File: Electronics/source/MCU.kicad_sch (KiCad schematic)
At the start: 48 parts, among them J1 Conn_01x05, J16 Conn_01x02, J2 Conn_01x03, J3 Conn_01x03, J4 Conn_01x05, J6 Conn_01x20, J7 Conn_01x20, SW10 SW_Push, SW11 SW_Push, SW12 SW_Push, SW13 SW_Push, SW14 SW_Coded, SW4 SW_Push, SW5 SW_SPDT, SW6 SW_SPDT, SW7 SW_SPDT, SW8 SW_Push, SW9 SW_Push, U1 STM32F030C8Tx, U4 FT231XS, U5 ADP122AUJZ-3.3-R7, Y1 ABL-32.000MHZ-B2

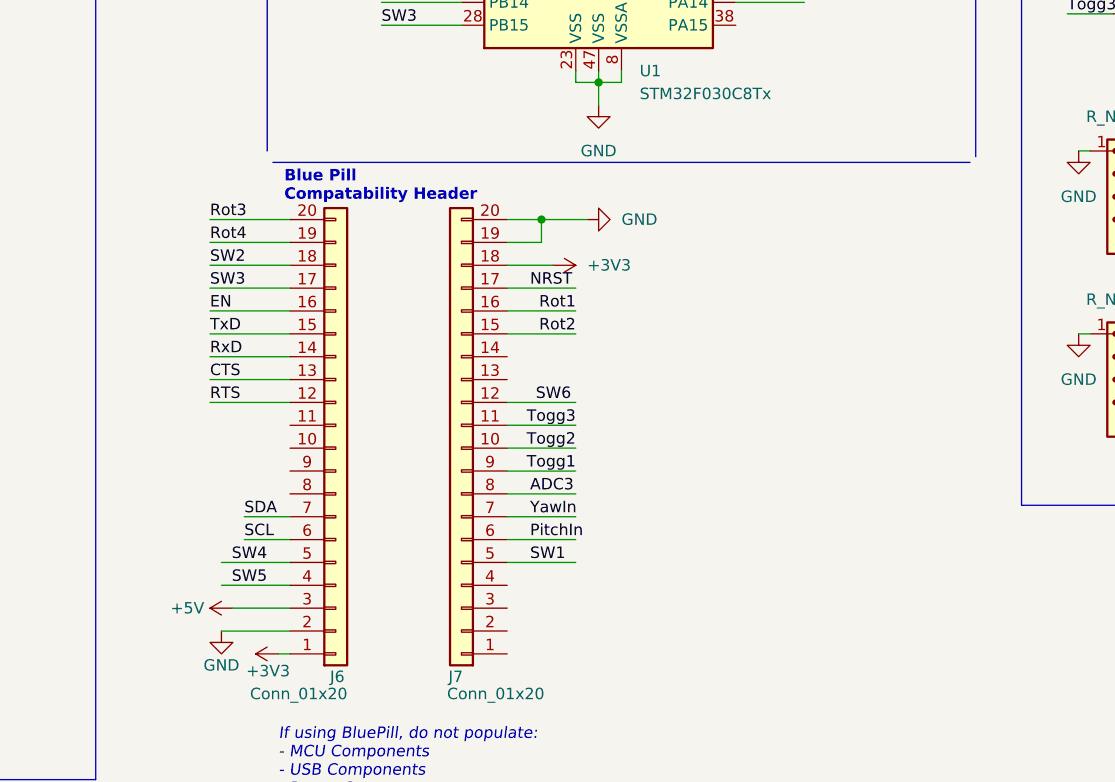
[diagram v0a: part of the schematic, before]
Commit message: Finished first layout of all boards
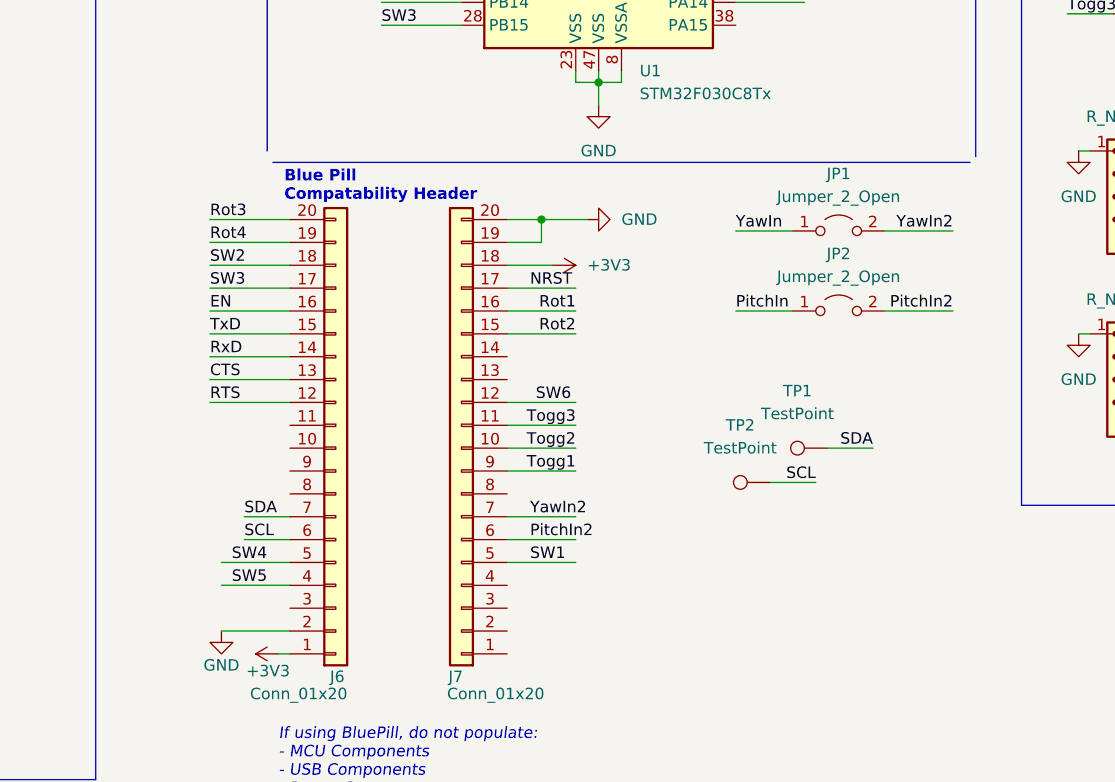
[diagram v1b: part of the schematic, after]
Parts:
- added JP1, JP2: Jumper_2_Open, Jumper:SolderJumper-2_P1.3mm_Open_TrianglePad1.0x1.5mm, symbol Jumper:Jumper_2_Open
- added TP1, TP2: TestPoint, TestPoint:TestPoint_Pad_D1.0mm, symbol Connector:TestPoint
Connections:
- net +5V: no longer J6.3 (Pin_3)
- net ADC3: no longer J7.8 (Pin_8)
- net PitchIn: now also JP2.1 (A); no longer J7.6 (Pin_6)
- net SCL: now also TP2.1
- net SDA: now also TP1.1
- net YawIn: now also JP1.1 (A); no longer J7.7 (Pin_7)
- new net PitchIn2: J7.6 (Pin_6), JP2.2 (B)
- new net YawIn2: J7.7 (Pin_7), JP1.2 (B)
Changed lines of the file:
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@@
-    (stroke (width 0) (type default) (color 0 0 0 0))
-  )
-  (wire (pts (xy 111.76 173.99) (xy 105.41 173.99))
     (stroke (width 0) (type default) (color 0 0 0 0))
   )
@@
     (stroke (width 0) (type default) (color 0 0 0 0))
   )
+  (wire (pts (xy 161.29 140.97) (xy 167.64 140.97))
+    (stroke (width 0) (type default) (color 0 0 0 0))
+  )
   (wire (pts (xy 121.92 66.04) (xy 130.81 66.04))
     (stroke (width 0) (type default) (color 0 0 0 0))
@@
     (stroke (width 0) (type default) (color 0 0 0 0))
   )
+  (wire (pts (xy 177.8 132.08) (xy 185.42 132.08))
+    (stroke (width 0) (type default) (color 0 0 0 0))
+  )
   (wire (pts (xy 161.29 73.66) (xy 168.91 73.66))
     (stroke (width 0) (type default) (color 0 0 0 0))
@@
     (stroke (width 0) (type default) (color 0 0 0 0))
   )
+  (wire (pts (xy 165.1 160.02) (xy 170.18 160.02))
+    (stroke (width 0) (type default) (color 0 0 0 0))
+  )
   (wire (pts (xy 161.29 106.68) (xy 168.91 106.68))
     (stroke (width 0) (type default) (color 0 0 0 0))
@@
     (stroke (width 0) (type default) (color 0 0 0 0))
   )
+  (wire (pts (xy 177.8 140.97) (xy 185.42 140.97))
+    (stroke (width 0) (type default) (color 0 0 0 0))
+  )
   (wire (pts (xy 194.31 44.45) (xy 203.2 44.45))
     (stroke (width 0) (type default) (color 0 0 0 0))
@@
     (stroke (width 0) (type default) (color 0 0 0 0))
   )
+  (wire (pts (xy 161.29 132.08) (xy 167.64 132.08))
+    (stroke (width 0) (type default) (color 0 0 0 0))
+  )
   (wire (pts (xy 102.87 135.89) (xy 111.76 135.89))
     (stroke (width 0) (type default) (color 0 0 0 0))
@@
     (stroke (width 0) (type default) (color 0 0 0 0))
   )
+  (wire (pts (xy 171.45 156.21) (xy 176.53 156.21))
+    (stroke (width 0) (type default) (color 0 0 0 0))
+  )
   (wire (pts (xy 121.92 73.66) (xy 130.81 73.66))
     (stroke (width 0) (type default) (color 0 0 0 0))
@@
   )
   (wire (pts (xy 148.59 115.57) (xy 146.05 115.57))
-    (stroke (width 0) (type default) (color 0 0 0 0))
-  )
-  (wire (pts (xy 135.89 161.29) (xy 143.51 161.29))
     (stroke (width 0) (type default) (color 0 0 0 0))
   )
@@
     (effects (font (size 1.27 1.27)) (justify left bottom))
   )
+  (label "PitchIn2" (at 185.42 140.97 180)
+    (effects (font (size 1.27 1.27)) (justify right bottom))
+  )
   (label "Togg2" (at 143.51 156.21 180)
     (effects (font (size 1.27 1.27)) (justify right bottom))
   )
-  (label "PitchIn" (at 138.43 166.37 0)
+  (label "PitchIn2" (at 138.43 166.37 0)
     (effects (font (size 1.27 1.27)) (justify left bottom))
   )
@@
     (effects (font (size 1.27 1.27)) (justify right bottom))
   )
-  (label "YawIn" (at 138.43 163.83 0)
+  (label "YawIn" (at 161.29 132.08 0)
+    (effects (font (size 1.27 1.27)) (justify left bottom))
+  )
+  (label "SCL" (at 170.18 160.02 180)
+    (effects (font (size 1.27 1.27)) (justify right bottom))
+  )
+  (label "YawIn2" (at 138.43 163.83 0)
     (effects (font (size 1.27 1.27)) (justify left bottom))
   )
@@
     (effects (font (size 1.27 1.27)) (justify left bottom))
   )
+  (label "YawIn2" (at 185.42 132.08 180)
+    (effects (font (size 1.27 1.27)) (justify right bottom))
+  )
   (label "USB_DM" (at 76.2 96.52 0)
     (effects (font (size 1.27 1.27)) (justify left bottom))
@@
   (label "3v3Out" (at 29.21 144.78 0)
     (effects (font (size 1.27 1.27)) (justify left bottom))
+  )
+  (label "SDA" (at 176.53 156.21 180)
+    (effects (font (size 1.27 1.27)) (justify right bottom))
   )
   (label "GND" (at 203.2 27.94 180)
@@
     (effects (font (size 1.27 1.27)) (justify left bottom))
   )
-  (label "ADC3" (at 138.43 161.29 0)
-    (effects (font (size 1.27 1.27)) (justify left bottom))
-  )
   (label "SW6" (at 259.08 154.94 0)
+    (effects (font (size 1.27 1.27)) (justify left bottom))
+  )
+  (label "PitchIn" (at 161.29 140.97 0)
     (effects (font (size 1.27 1.27)) (justify left bottom))
   )
@@
   (label "SDA" (at 203.2 22.86 180)
     (effects (font (size 1.27 1.27)) (justify right bottom))
+  )
+  (symbol (lib_id "Connector:TestPoint") (at 165.1 160.02 90) (unit 1)
+    (in_bom yes) (on_board yes) (fields_autoplaced)
+    (property "Reference" "TP2" (id 0) (at 161.798 153.67 90))
+    (property "Value" "TestPoint" (id 1) (at 161.798 156.21 90))
+    (property "Footprint" "TestPoint:TestPoint_Pad_D1.0mm" (id 2) (at 165.1 154.94 0)
+      (effects (font (size 1.27 1.27)) hide)
+    )
+    (property "Datasheet" "~" (id 3) (at 165.1 154.94 0)
+      (effects (font (size 1.27 1.27)) hide)
+    )
+    (pin "1")
   )
   (symbol (lib_id "Device:R_Network05") (at 205.74 148.59 90) (mirror x) (unit 1)
@@
     (pin "2")
   )
+  (symbol (lib_id "Jumper:Jumper_2_Open") (at 172.72 140.97 0) (unit 1)
+    (in_bom yes) (on_board yes) (fields_autoplaced)
+    (property "Reference" "JP2" (id 0) (at 172.72 134.62 0))
+    (property "Value" "Jumper_2_Open" (id 1) (at 172.72 137.16 0))
+    (property "Footprint" "Jumper:SolderJumper-2_P1.3mm_Open_TrianglePad1.0x1.5mm" (id 2) (at 172.72 140.97 0)
+      (effects (font (size 1.27 1.27)) hide)
+    )
+    (property "Datasheet" "~" (id 3) (at 172.72 140.97 0)
+      (effects (font (size 1.27 1.27)) hide)
+    )
+    (pin "1")
+    (pin "2")
+  )
   (symbol (lib_id "Device:C") (at 124.46 27.94 0) (unit 1)
     (in_bom yes) (on_board yes)
@@
     )
     (pin "1")
+  )
+  (symbol (lib_id "Jumper:Jumper_2_Open") (at 172.72 132.08 0) (unit 1)
+    (in_bom yes) (on_board yes) (fields_autoplaced)
+    (property "Reference" "JP1" (id 0) (at 172.72 125.73 0))
+    (property "Value" "Jumper_2_Open" (id 1) (at 172.72 128.27 0))
+    (property "Footprint" "Jumper:SolderJumper-2_P1.3mm_Open_TrianglePad1.0x1.5mm" (id 2) (at 172.72 132.08 0)
+      (effects (font (size 1.27 1.27)) hide)
+    )
+    (property "Datasheet" "~" (id 3) (at 172.72 132.08 0)
+      (effects (font (size 1.27 1.27)) hide)
+    )
+    (pin "1")
+    (pin "2")
   )
   (symbol (lib_id "Device:C") (at 171.45 27.94 0) (unit 1)
@@
     (pin "1")
   )
-  (symbol (lib_id "power:+5V") (at 105.41 173.99 90) (unit 1)
-    (in_bom yes) (on_board yes) (fields_autoplaced)
-    (property "Reference" "#PWR0154" (id 0) (at 109.22 173.99 0)
-      (effects (font (size 1.27 1.27)) hide)
-    )
-    (property "Value" "+5V" (id 1) (at 102.235 173.9899 90)
-      (effects (font (size 1.27 1.27)) (justify left))
-    )
-    (property "Footprint" "" (id 2) (at 105.41 173.99 0)
-      (effects (font (size 1.27 1.27)) hide)
-    )
-    (property "Datasheet" "" (id 3) (at 105.41 173.99 0)
-      (effects (font (size 1.27 1.27)) hide)
-    )
-    (pin "1")
-  )
   (symbol (lib_id "power:GND") (at 171.45 31.75 0) (unit 1)
     (in_bom yes) (on_board yes) (fields_autoplaced)
@@
     (pin "2")
   )
+  (symbol (lib_id "Connector:TestPoint") (at 171.45 156.21 90) (unit 1)
+    (in_bom yes) (on_board yes) (fields_autoplaced)
+    (property "Reference" "TP1" (id 0) (at 168.148 149.86 90))
+    (property "Value" "TestPoint" (id 1) (at 168.148 152.4 90))
+    (property "Footprint" "TestPoint:TestPoint_Pad_D1.0mm" (id 2) (at 171.45 151.13 0)
+      (effects (font (size 1.27 1.27)) hide)
+    )
+    (property "Datasheet" "~" (id 3) (at 171.45 151.13 0)
+      (effects (font (size 1.27 1.27)) hide)
+    )
+    (pin "1")
+  )
   (symbol (lib_id "power:GND") (at 111.76 41.91 0) (unit 1)

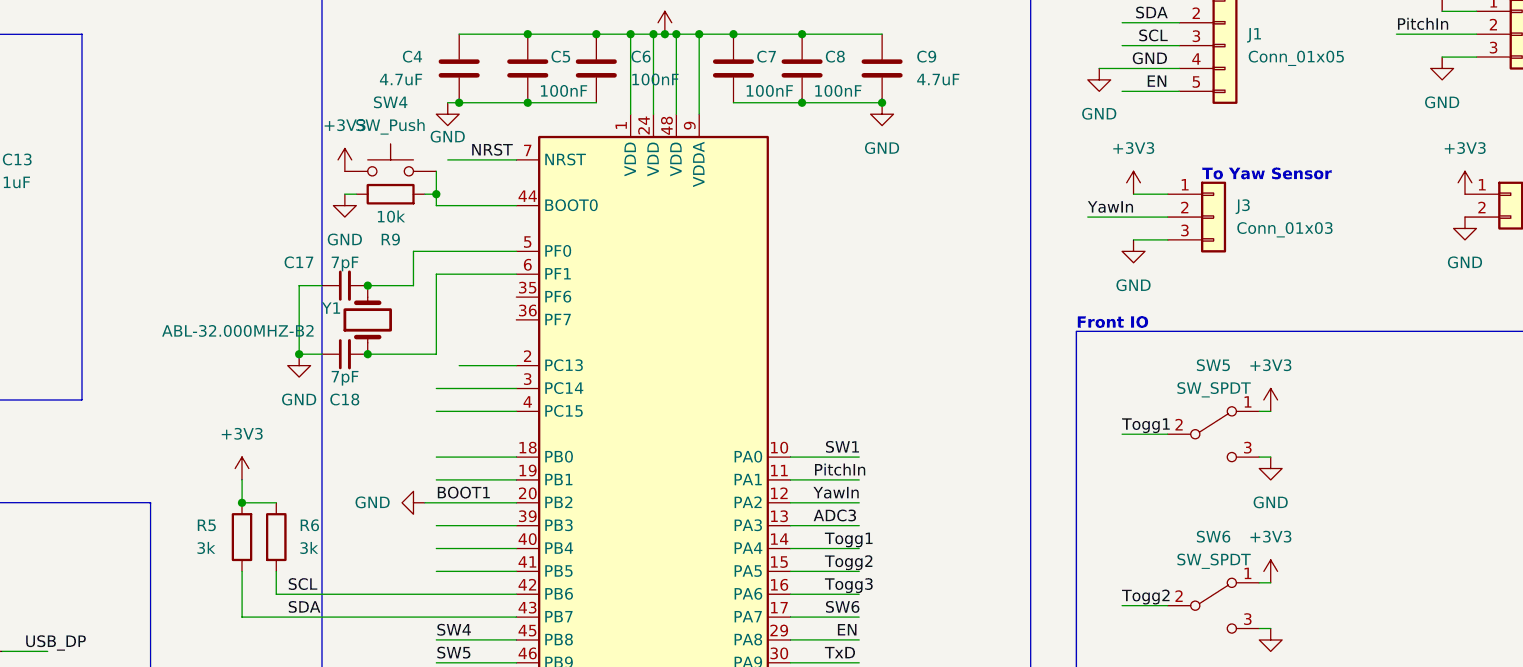
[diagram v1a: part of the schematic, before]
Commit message: Made PCB manufacturable and finished *-rounded silk
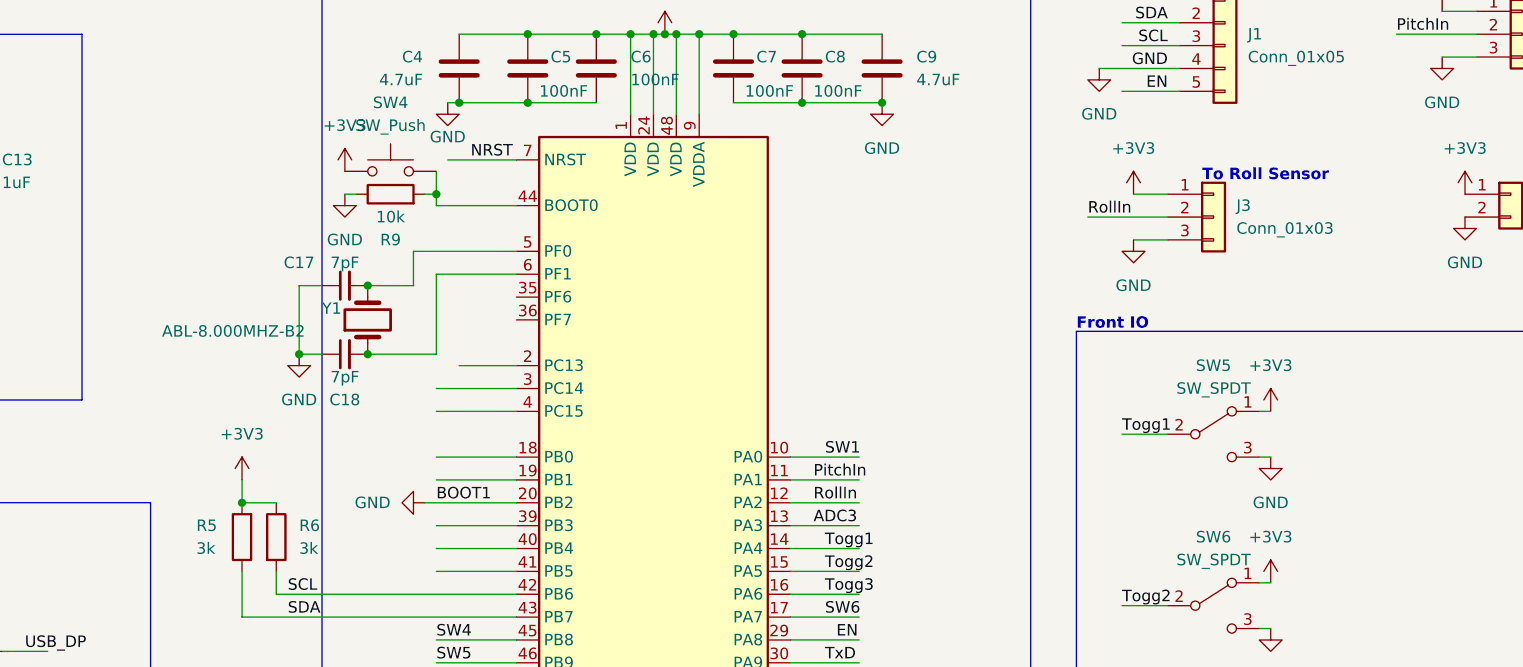
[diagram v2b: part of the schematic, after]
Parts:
- Y1: value ABL-32.000MHZ-B2 -> ABL-8.000MHZ-B2
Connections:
- net YawIn: no longer J3.2 (Pin_2), U1.12 (PA2)
- new net RollIn: J3.2 (Pin_2), U1.12 (PA2)
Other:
- note added: "To Roll Sensor"
- note removed: "To Yaw Sensor"
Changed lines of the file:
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@@
     (effects (font (size 1.27 1.27) (thickness 0.254) bold) (justify left bottom))
   )
-  (text "To Yaw Sensor" (at 207.01 40.64 0)
+  (text "To Roll Sensor" (at 207.01 40.64 0)
     (effects (font (size 1.27 1.27) bold) (justify left bottom))
   )
@@
     (effects (font (size 1.27 1.27)) (justify left bottom))
   )
-  (label "YawIn" (at 194.31 44.45 0)
+  (label "RollIn" (at 194.31 44.45 0)
     (effects (font (size 1.27 1.27)) (justify left bottom))
   )
@@
     (effects (font (size 1.27 1.27)) (justify left bottom))
   )
-  (label "YawIn" (at 163.83 76.2 0)
+  (label "RollIn" (at 163.83 76.2 0)
     (effects (font (size 1.27 1.27)) (justify left bottom))
   )
@@
       (effects (font (size 1.27 1.27)) (justify right))
     )
-    (property "Value" "ABL-32.000MHZ-B2" (id 1) (at 91.44 57.15 90)
+    (property "Value" "ABL-8.000MHZ-B2" (id 1) (at 91.44 57.15 90)
       (effects (font (size 1.27 1.27)) (justify right))
     )

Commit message: finished rev0.1 of PCBs
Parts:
- Y1: footprint Crystal:Crystal_HC49-U_Vertical -> Crystal:Crystal_HC49-4H_Vertical
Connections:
- net YawIn is gone; now on net RollIn: JP1.1 (A)
- net YawIn2 renamed RollIn2
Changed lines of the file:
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@@
     (effects (font (size 1.27 1.27)) (justify right bottom))
   )
-  (label "YawIn" (at 161.29 132.08 0)
+  (label "RollIn" (at 161.29 132.08 0)
     (effects (font (size 1.27 1.27)) (justify left bottom))
   )
@@
     (effects (font (size 1.27 1.27)) (justify right bottom))
   )
-  (label "YawIn2" (at 138.43 163.83 0)
+  (label "RollIn2" (at 138.43 163.83 0)
     (effects (font (size 1.27 1.27)) (justify left bottom))
   )
@@
     (effects (font (size 1.27 1.27)) (justify left bottom))
   )
-  (label "YawIn2" (at 185.42 132.08 180)
+  (label "RollIn2" (at 185.42 132.08 180)
     (effects (font (size 1.27 1.27)) (justify right bottom))
   )
@@
       (effects (font (size 1.27 1.27)) (justify right))
     )
-    (property "Footprint" "Crystal:Crystal_HC49-U_Vertical" (id 2) (at 114.3 55.88 0)
-      (effects (font (size 1.27 1.27)) hide)
-    )
+    (property "Footprint" "Crystal:Crystal_HC49-4H_Vertical" (id 2) (at 114.3 55.88 0)
+      (effects (font (size 1.27 1.27)) hide)
+    )
